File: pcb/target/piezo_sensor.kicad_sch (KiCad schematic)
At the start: 4 parts, among them J3 Piezo

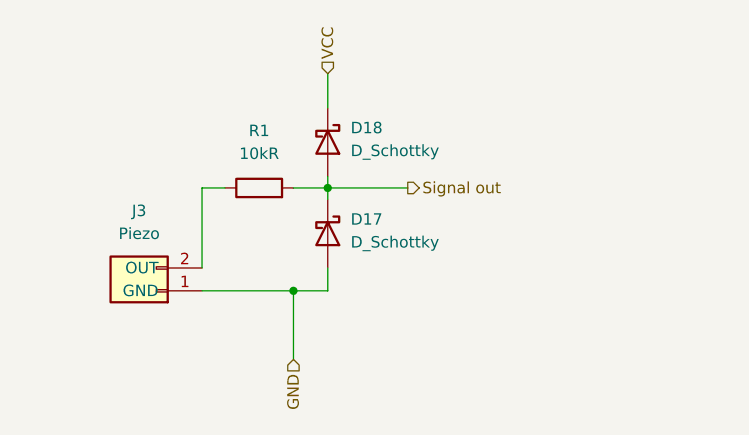
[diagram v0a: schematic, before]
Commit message: added updi connector
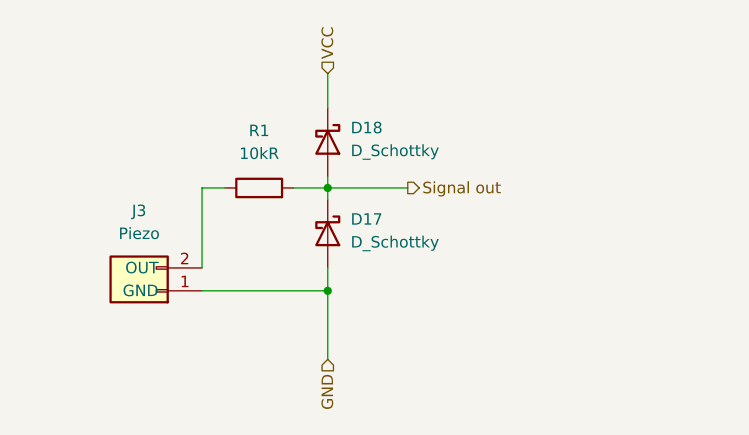
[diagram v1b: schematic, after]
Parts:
- J3: footprint (none) -> Connector_Wire:SolderWire-0.1sqmm_1x02_P3.6mm_D0.4mm_OD1mm
- R1: footprint (none) -> Resistor_SMD:R_1206_3216Metric
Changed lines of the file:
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@@
 	(paper "A4")
 	(junction
-		(at 91.44 81.28)
+		(at 95.25 81.28)
 		(diameter 0)
 		(color 0 0 0 0)
@@
 	(wire
 		(pts
-			(xy 91.44 81.28) (xy 95.25 81.28)
-		)
-		(stroke
-			(width 0)
-			(type default)
-		)
-	)
-	(wire
-		(pts
 			(xy 95.25 69.85) (xy 95.25 71.12)
 		)
@@
 	(wire
 		(pts
-			(xy 81.28 81.28) (xy 91.44 81.28)
-		)
-		(stroke
-			(width 0)
-			(type default)
-		)
-	)
-	(wire
-		(pts
-			(xy 91.44 81.28) (xy 91.44 88.9)
+			(xy 81.28 81.28) (xy 95.25 81.28)
+		)
+		(stroke
+			(width 0)
+			(type default)
+		)
+	)
+	(wire
+		(pts
+			(xy 95.25 81.28) (xy 95.25 88.9)
 		)
 		(stroke
@@
 	(hierarchical_label "GND"
 		(shape input)
-		(at 91.44 88.9 270)
+		(at 95.25 88.9 270)
 		(effects
 			(font
@@
 			)
 		)
-		(property "Footprint" ""
+		(property "Footprint" "Resistor_SMD:R_1206_3216Metric"
 			(at 87.63 71.628 90)
 			(effects
@@
 			)
 		)
-		(property "Footprint" ""
+		(property "Footprint" "Connector_Wire:SolderWire-0.1sqmm_1x02_P3.6mm_D0.4mm_OD1mm"
 			(at 76.2 81.28 0)
 			(effects

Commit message: fixed some footprint issues
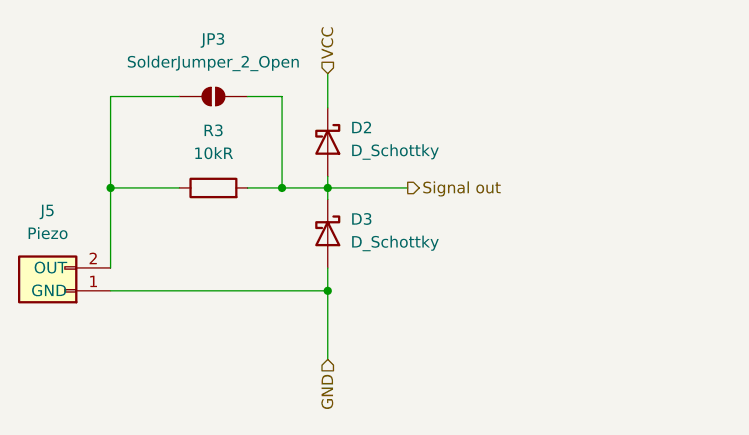
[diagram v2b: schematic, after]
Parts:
- added JP3: SolderJumper_2_Open, Jumper:SolderJumper-2_P1.3mm_Open_TrianglePad1.0x1.5mm, symbol Jumper:SolderJumper_2_Open
- renumbered D18 to D2, D17 to D3, J3 to J5, R1 to R3
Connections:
- net Signal out: now also JP3.2 (B)
- net at J5.2 (OUT), R3.1: now also JP3.1 (A)
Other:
- moved on the sheet: J5, R3
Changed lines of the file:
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@@
 	(paper "A4")
+	(junction
+		(at 71.12 69.85)
+		(diameter 0)
+		(color 0 0 0 0)
+	)
 	(junction
 		(at 95.25 81.28)
@@
 		(color 0 0 0 0)
 	)
-	(wire
-		(pts
-			(xy 81.28 69.85) (xy 83.82 69.85)
-		)
-		(stroke
-			(width 0)
-			(type default)
-		)
-	)
-	(wire
-		(pts
-			(xy 91.44 69.85) (xy 95.25 69.85)
+	(junction
+		(at 90.17 69.85)
+		(diameter 0)
+		(color 0 0 0 0)
+	)
+	(wire
+		(pts
+			(xy 71.12 69.85) (xy 78.74 69.85)
+		)
+		(stroke
+			(width 0)
+			(type default)
+		)
+	)
+	(wire
+		(pts
+			(xy 86.36 69.85) (xy 90.17 69.85)
 		)
 		(stroke
@@
 	(wire
 		(pts
-			(xy 81.28 69.85) (xy 81.28 78.74)
+			(xy 71.12 69.85) (xy 71.12 78.74)
 		)
 		(stroke
@@
 	(wire
 		(pts
-			(xy 81.28 81.28) (xy 95.25 81.28)
+			(xy 71.12 69.85) (xy 71.12 59.69)
+		)
+		(stroke
+			(width 0)
+			(type default)
+		)
+	)
+	(wire
+		(pts
+			(xy 71.12 59.69) (xy 78.74 59.69)
+		)
+		(stroke
+			(width 0)
+			(type default)
+		)
+	)
+	(wire
+		(pts
+			(xy 86.36 59.69) (xy 90.17 59.69)
+		)
+		(stroke
+			(width 0)
+			(type default)
+		)
+	)
+	(wire
+		(pts
+			(xy 71.12 81.28) (xy 95.25 81.28)
+		)
+		(stroke
+			(width 0)
+			(type default)
+		)
+	)
+	(wire
+		(pts
+			(xy 90.17 69.85) (xy 95.25 69.85)
+		)
+		(stroke
+			(width 0)
+			(type default)
+		)
+	)
+	(wire
+		(pts
+			(xy 90.17 59.69) (xy 90.17 69.85)
 		)
 		(stroke
@@
 		(dnp no)
 		(fields_autoplaced yes)
-		(property "Reference" "D18"
+		(property "Reference" "D2"
 			(at 97.79 63.1824 90)
 			(effects
@@
 			(project ""
 				(path "/1c02f793-f381-44cb-838a-dbb787484d0c/fa4a9502-947a-474b-a67c-c6d6a6dcf435"
-					(reference "D18")
+					(reference "D2")
 					(unit 1)
 				)
@@
 	(symbol
 		(lib_id "Device:R")
-		(at 87.63 69.85 90)
+		(at 82.55 69.85 90)
 		(unit 1)
 		(exclude_from_sim no)
@@
 		(dnp no)
 		(fields_autoplaced yes)
-		(property "Reference" "R1"
-			(at 87.63 63.5 90)
+		(property "Reference" "R3"
+			(at 82.55 63.5 90)
 			(effects
 				(font
@@
 		)
 		(property "Value" "10kR"
-			(at 87.63 66.04 90)
+			(at 82.55 66.04 90)
 			(effects
 				(font
@@
 		)
 		(property "Footprint" "Resistor_SMD:R_1206_3216Metric"
-			(at 87.63 71.628 90)
+			(at 82.55 71.628 90)
 			(effects
 				(font
@@
 		)
 		(property "Datasheet" "~"
-			(at 87.63 69.85 0)
+			(at 82.55 69.85 0)
 			(effects
 				(font
@@
 		)
 		(property "Description" "Resistor"
-			(at 87.63 69.85 0)
+			(at 82.55 69.85 0)
 			(effects
 				(font
@@
 			(project ""
 				(path "/1c02f793-f381-44cb-838a-dbb787484d0c/fa4a9502-947a-474b-a67c-c6d6a6dcf435"
-					(reference "R1")
+					(reference "R3")
 					(unit 1)
 				)
@@
 		(dnp no)
 		(fields_autoplaced yes)
-		(property "Reference" "D17"
+		(property "Reference" "D3"
 			(at 97.79 73.3424 90)
 			(effects
@@
 			(project ""
 				(path "/1c02f793-f381-44cb-838a-dbb787484d0c/fa4a9502-947a-474b-a67c-c6d6a6dcf435"
-					(reference "D17")
+					(reference "D3")
 					(unit 1)
 				)
@@
 	(symbol
 		(lib_id "Connector_Generic:Conn_01x02")
-		(at 76.2 81.28 180)
+		(at 66.04 81.28 180)
 		(unit 1)
 		(exclude_from_sim no)
@@
 		(dnp no)
 		(fields_autoplaced yes)
-		(property "Reference" "J3"
-			(at 74.295 72.39 0)
+		(property "Reference" "J5"
+			(at 64.135 72.39 0)
 			(effects
 				(font
@@
 		)
 		(property "Value" "Piezo"
-			(at 74.295 74.93 0)
+			(at 64.135 74.93 0)
 			(effects
 				(font
@@
 		)
 		(property "Footprint" "Connector_Wire:SolderWire-0.1sqmm_1x02_P3.6mm_D0.4mm_OD1mm"
-			(at 76.2 81.28 0)
+			(at 66.04 81.28 0)
 			(effects
 				(font
@@
 		)
 		(property "Datasheet" "~"
-			(at 76.2 81.28 0)
+			(at 66.04 81.28 0)
 			(effects
 				(font
@@
 		)
 		(property "Description" "Generic connector, single row, 01x02, script generated (kicad-library-utils/schlib/autogen/connector/)"
-			(at 76.2 81.28 0)
+			(at 66.04 81.28 0)
 			(effects
 				(font
@@
 			(project "target"
 				(path "/1c02f793-f381-44cb-838a-dbb787484d0c/fa4a9502-947a-474b-a67c-c6d6a6dcf435"
-					(reference "J3")
+					(reference "J5")
 					(unit 1)
 				)
+			)
+		)
+	)
+	(symbol
+		(lib_id "Jumper:SolderJumper_2_Open")
+		(at 82.55 59.69 0)
+		(unit 1)
+		(exclude_from_sim no)
+		(in_bom no)
+		(on_board yes)
+		(dnp no)
+		(fields_autoplaced yes)
+		(property "Reference" "JP3"
+			(at 82.55 53.34 0)
+			(effects
+				(font
+					(size 1.27 1.27)
+				)
+			)
+		)
+		(property "Value" "SolderJumper_2_Open"
+			(at 82.55 55.88 0)
+			(effects
+				(font
+					(size 1.27 1.27)
+				)
+			)
+		)
+		(property "Footprint" "Jumper:SolderJumper-2_P1.3mm_Open_TrianglePad1.0x1.5mm"
+			(at 82.55 59.69 0)
+			(effects
+				(font
+					(size 1.27 1.27)
+				)
+				(hide yes)
+			)
+		)
+		(property "Datasheet" "~"
+			(at 82.55 59.69 0)
+			(effects
+				(font
+					(size 1.27 1.27)
+				)
+				(hide yes)
+			)
+		)
+		(property "Description" "Solder Jumper, 2-pole, open"
+			(at 82.55 59.69 0)
+			(effects
+				(font
+					(size 1.27 1.27)
+				)
+				(hide yes)
+			)
+		)
+		(pin "1"
+		)
+		(pin "2"
+		)
+		(instances
+			(project ""
+				(path "/1c02f793-f381-44cb-838a-dbb787484d0c/fa4a9502-947a-474b-a67c-c6d6a6dcf435"
+					(reference "JP3")
+					(unit 1)
+				)

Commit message: added lcsc numbers to all components and added ESD protection
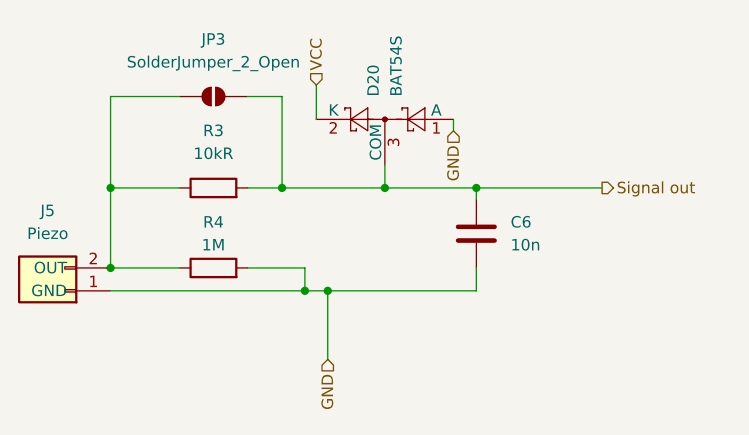
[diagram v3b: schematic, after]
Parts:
- removed D2, D3: D_Schottky, custom_footprints:BAT54_SOT23, symbol Device:D_Schottky
- added C6: 10n, Capacitor_SMD:C_0805_2012Metric, symbol Device:C
- added D20: BAT54S, Package_TO_SOT_SMD:SOT-23, symbol Diode:BAT54S
- added R4: 1M, Resistor_SMD:R_0805_2012Metric, symbol Device:R
- R3: footprint Resistor_SMD:R_1206_3216Metric -> Resistor_SMD:R_0805_2012Metric; LCSC (none) -> C84376
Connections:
- net GND: now also C6.2, D20.1 (A), R4.2
- net Signal out: now also C6.1, D20.3 (COM)
- net VCC: now also D20.2 (K)
- net at J5.2 (OUT), JP3.1 (A), R3.1: now also R4.1

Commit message: finished all pcbs by adjusting traces acording to 1oz copper weight
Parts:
- J5: now left out of the parts list
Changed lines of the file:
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@@
 		(unit 1)
 		(exclude_from_sim no)
-		(in_bom yes)
+		(in_bom no)
 		(on_board yes)
 		(dnp no)
